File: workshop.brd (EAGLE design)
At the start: 50 x 80 mm, 8 parts, among them IC1 LM555N

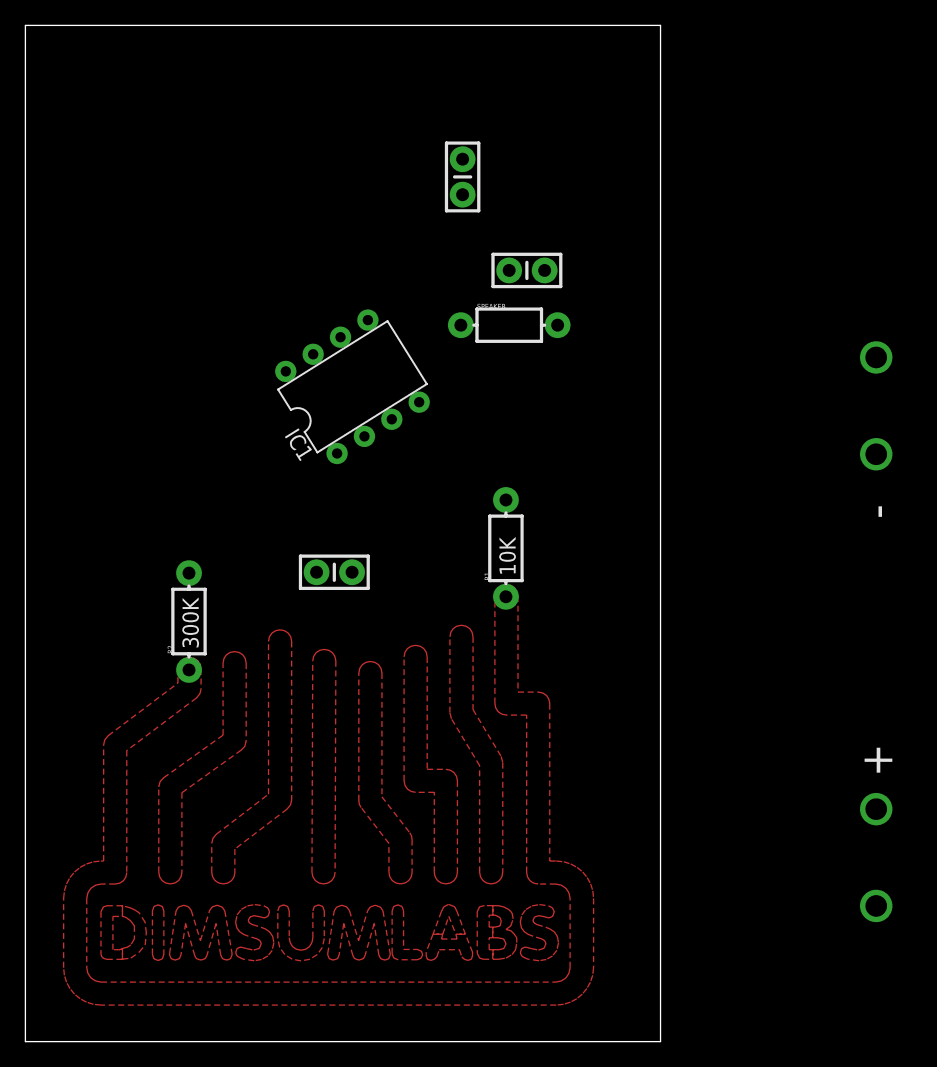
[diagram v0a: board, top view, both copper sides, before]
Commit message: Simpler version with LED and switch
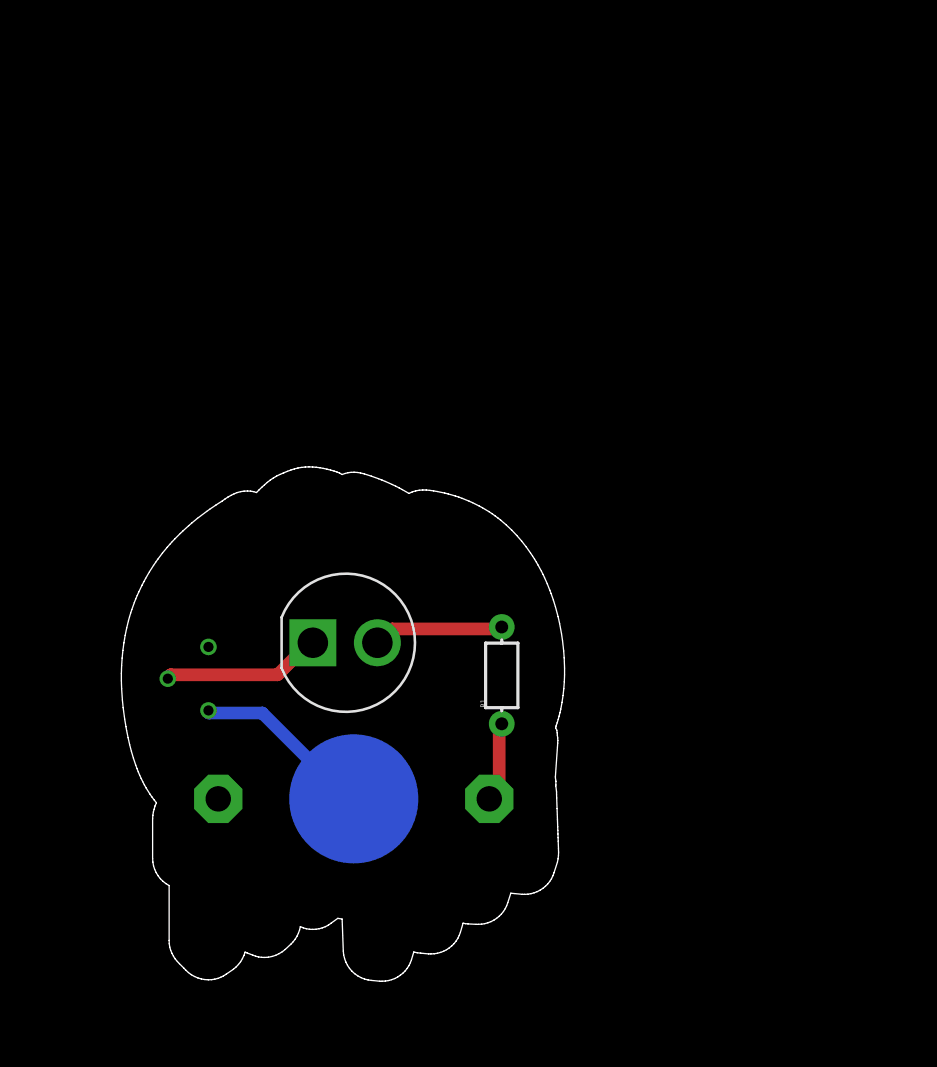
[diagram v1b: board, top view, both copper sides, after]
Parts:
- removed BAT1: (no value), SparkFun-Electromechanical:BATTERY-AAA
- removed C1: 0.01uF, SparkFun-Capacitors:CAP-PTH-SMALL-KIT
- removed C2: 680pF, SparkFun-Capacitors:CAP-PTH-SMALL-KIT
- removed C3: (no value), SparkFun-Capacitors:CAP-PTH-SMALL-KIT
- removed IC1: LM555N, lio:DIL08-ROUND
- removed R2: 300K, SparkFun-Resistors:AXIAL-0.3-KIT
- removed SPEAKER: (no value), SparkFun-Resistors:AXIAL-0.3-KIT
- added D1: (no value), SparkFun-LED:LED10MM
- added S1: (no value), lio:MHS122
- added U$1: 219-7960, adafruit:CR2032-THRU
- R1: value 10K -> (none); device SparkFun-Resistors:AXIAL-0.3-KIT -> SparkFun-Passives:AXIAL-0.3-KIT
- moved R1 10.0 mm to (37.5, 28.8)
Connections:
- removed net COPPER: IC1.7, R1.P$1
- removed net N$21: R2.P$1
- removed net N$22: BAT1.PWR@1, IC1.4, IC1.8, R1.P$2
- removed net N$28: C1.1, IC1.5
- removed net N$29: C3.2, IC1.3
- removed net N$30: C3.1, SPEAKER.P$1
- removed net N$31: C2.1, IC1.2, IC1.6, R2.P$2
- new net N$1: D1.A, R1.P$2
- new net N$2: D1.C, S1.2
- new net N$3: R1.P$1, U$1.+2
- net GND: now also S1.1, U$1.-; no longer BAT1.GND@1, C1.2, C2.2, IC1.1, SPEAKER.P$2
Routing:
- net GND: track 0.00 -> 14.4 mm
- net N$2: track 0.00 -> 12.6 mm
- net N$1: track 0.00 -> 10.3 mm
- net N$3: track 0.00 -> 6.30 mm
- removed copper zone on layer 1, net COPPER
- removed copper zone on layer 1, net N$1
- removed copper zone on layer 1, net N$10
- removed copper zone on layer 1, net N$11
- removed copper zone on layer 1, net N$12
- removed copper zone on layer 1, net N$13
- removed copper zone on layer 1, net N$14
- removed copper zone on layer 1, net N$15
- removed copper zone on layer 1, net N$16
- removed copper zone on layer 1, net N$17
- removed copper zone on layer 1, net N$18
- removed copper zone on layer 1, net N$19
- removed copper zone on layer 1, net N$20
- removed copper zone on layer 1, net N$3
- removed copper zone on layer 1, net N$4
- removed copper zone on layer 1, net N$5
- removed copper zone on layer 1, net N$6
- removed copper zone on layer 1, net N$7
- removed copper zone on layer 1, net N$8
- removed copper zone on layer 1, net N$9
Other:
- board size 50 x 80 mm -> 34.9 x 40.5 mm

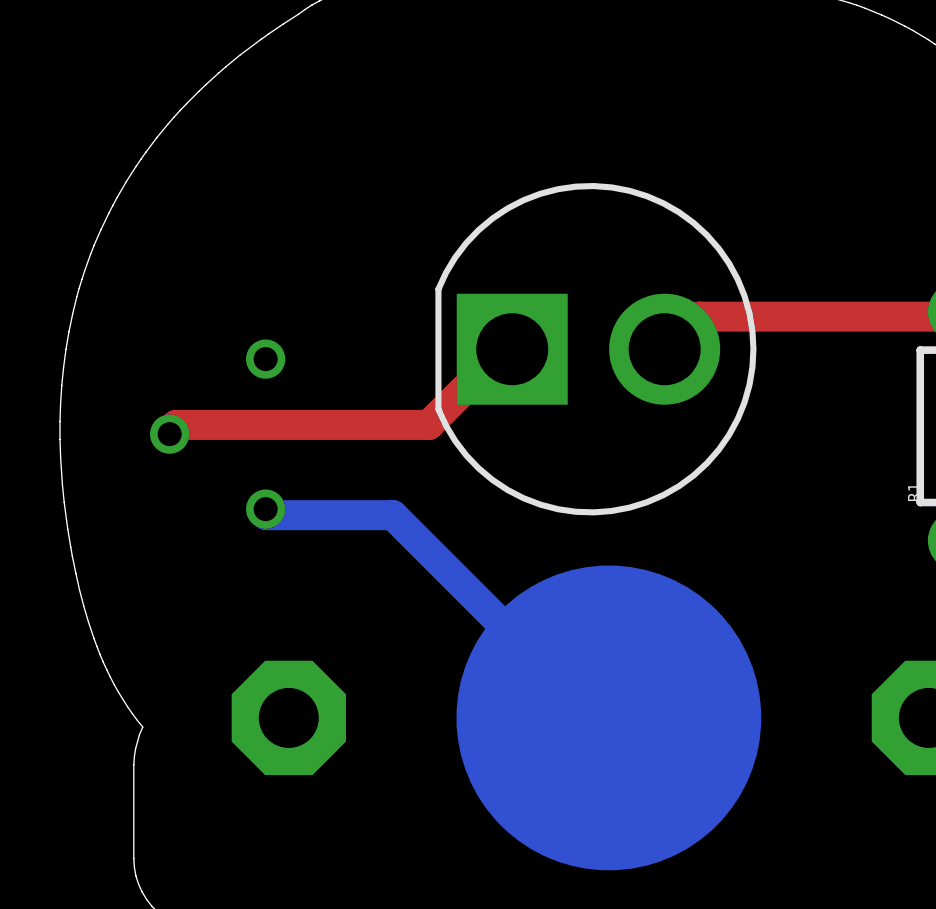
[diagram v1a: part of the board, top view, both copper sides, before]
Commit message: Fixed switch to MHS122-1 package
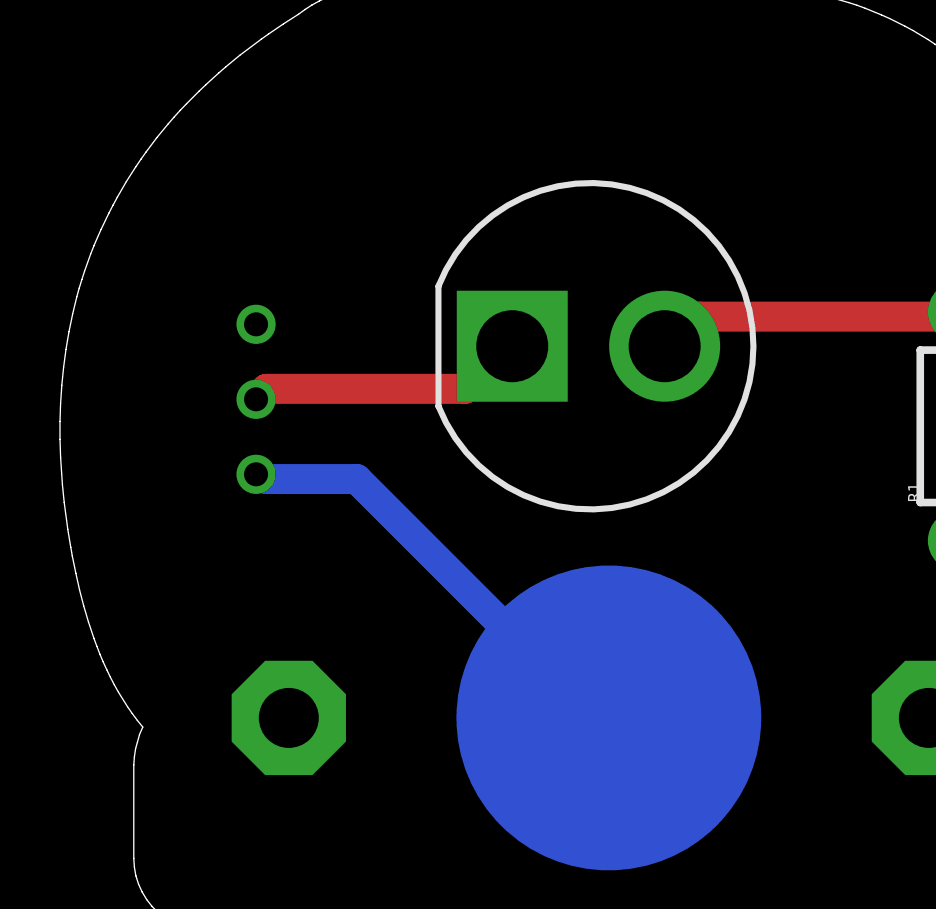
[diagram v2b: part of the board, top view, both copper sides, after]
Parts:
- S1: device lio:MHS122 -> lio:MHS122-1
- moved S1 1.73 mm to (14.1, 29.7)
- moved D1 0.10 mm to (25.2, 31.5)
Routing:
- net N$2: track 12.6 -> 9.24 mm
- net GND: track 14.4 -> 15.1 mm
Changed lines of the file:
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@@
 <board>
 <plain>
-<polygon width="0" layer="48">
+<polygon width="0" layer="51">
 <vertex x="11" y="22.205"/>
 <vertex x="36.33" y="22.205"/>
@@
 <vertex x="10.62" y="23.235"/>
 </polygon>
-<polygon width="0" layer="48">
+<polygon width="0" layer="51">
 <vertex x="11.02" y="22.205"/>
 <vertex x="11.11" y="21.825"/>
@@
 <vertex x="11.04" y="22.215"/>
 </polygon>
-<polygon width="0" layer="48">
+<polygon width="0" layer="51">
 <vertex x="37.17" y="22.205"/>
 <vertex x="39.24" y="22.205"/>
@@
 <elements>
 <element name="U$1" library="adafruit" package="CR2032-THRU" value="219-7960" x="25.85" y="19.11" rot="MR180"/>
-<element name="D1" library="SparkFun-LED" package="LED10MM" value="" x="25.17" y="31.4"/>
-<element name="S1" library="lio" package="MHS122" value="" x="12.81" y="28.57" rot="MR90"/>
+<element name="D1" library="SparkFun-LED" package="LED10MM" value="" x="25.17" y="31.5"/>
 <element name="R1" library="SparkFun-Passives" package="AXIAL-0.3-KIT" value="" x="37.5" y="28.83" rot="R90"/>
+<element name="S1" library="lio" package="MHS122-1" value="" x="14.09" y="29.73" rot="MR90"/>
 </elements>
 <signals>
@@
 <contactref element="U$1" pad="-"/>
 <contactref element="S1" pad="1"/>
-<wire x1="18.6496" y1="25.8688" x2="14.4384" y2="25.8688" width="1" layer="16"/>
-<wire x1="25.2672" y1="19.2512" x2="18.6496" y2="25.8688" width="1" layer="16"/>
-<wire x1="14.4384" y1="25.8688" x2="14.41" y2="26.07" width="1" layer="16"/>
+<wire x1="17.4464" y1="27.072" x2="14.4384" y2="27.072" width="1" layer="16"/>
+<wire x1="25.2672" y1="19.2512" x2="17.4464" y2="27.072" width="1" layer="16"/>
+<wire x1="14.4384" y1="27.072" x2="14.09" y2="27.23" width="1" layer="16"/>
 <wire x1="25.2672" y1="19.2512" x2="25.85" y2="19.11" width="1" layer="16"/>
 </signal>
@@
 <wire x1="28.2752" y1="31.8848" x2="28.8768" y2="32.4864" width="1" layer="1"/>
 <wire x1="37.2992" y1="32.4864" x2="37.5" y2="32.64" width="1" layer="1"/>
-<wire x1="28.2752" y1="31.8848" x2="27.71" y2="31.4" width="1" layer="1"/>
-</signal>
-<signal name="N$2">
-<contactref element="D1" pad="C"/>
-<contactref element="S1" pad="2"/>
-<wire x1="19.8528" y1="28.8768" x2="11.4304" y2="28.8768" width="1" layer="1"/>
-<wire x1="22.2592" y1="31.2832" x2="19.8528" y2="28.8768" width="1" layer="1"/>
-<wire x1="11.4304" y1="28.8768" x2="11.21" y2="28.57" width="1" layer="1"/>
-<wire x1="22.2592" y1="31.2832" x2="22.63" y2="31.4" width="1" layer="1"/>
+<wire x1="28.2752" y1="31.8848" x2="27.71" y2="31.5" width="1" layer="1"/>
 </signal>
 <signal name="N$3">
@@
 <wire x1="36.6976" y1="19.2512" x2="36.518" y2="19.11" width="1" layer="1"/>
 </signal>
+<signal name="N$2">
+<contactref element="D1" pad="C"/>
+<contactref element="S1" pad="2"/>
+<wire x1="21.056" y1="30.08" x2="14.4384" y2="30.08" width="1" layer="1"/>
+<wire x1="22.2592" y1="31.2832" x2="21.056" y2="30.08" width="1" layer="1"/>
+<wire x1="14.4384" y1="30.08" x2="14.09" y2="29.73" width="1" layer="1"/>
+<wire x1="22.2592" y1="31.2832" x2="22.63" y2="31.5" width="1" layer="1"/>
+</signal>
 </signals>
